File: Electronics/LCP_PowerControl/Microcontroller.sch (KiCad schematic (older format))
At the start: 24 parts, among them J5 Conn_02x05_Odd_Even, SW1 SW_Push, U3 MSP430FR5989, Y1 32.768kHz

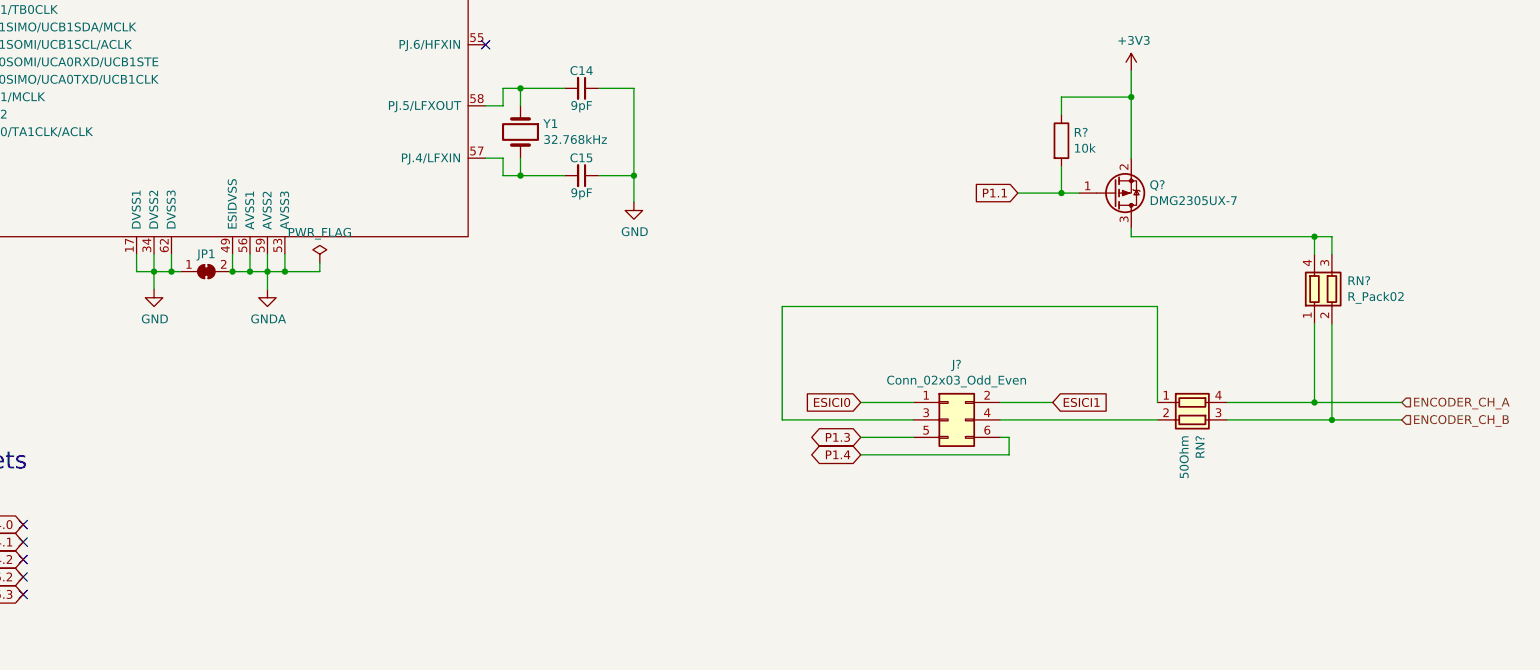
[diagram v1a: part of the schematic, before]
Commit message: Rev1.1 Gerber Upload
Included 3way open solder jumps to choose control of Encoder channels of hall effect sensor
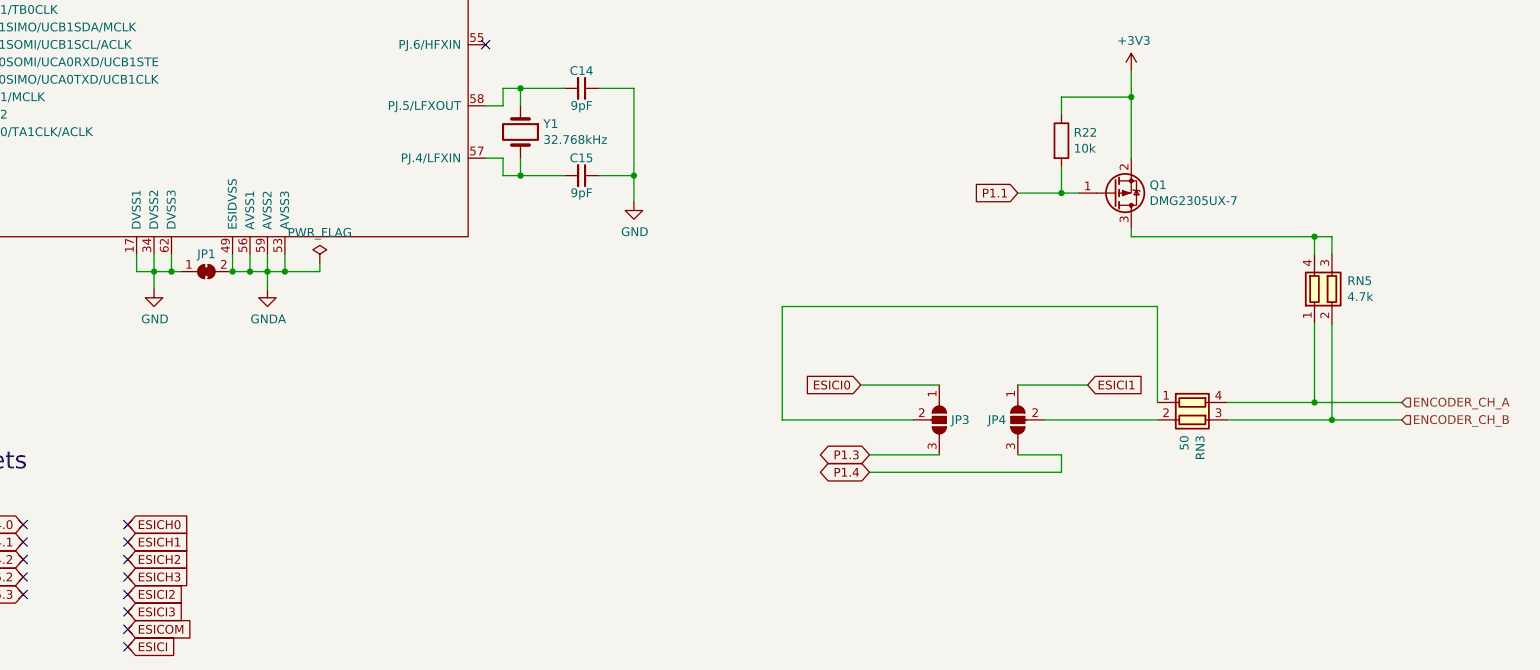
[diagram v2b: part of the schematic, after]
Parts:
- removed J?: Conn_02x03_Odd_Even, Connector_PinHeader_2.54mm:PinHeader_2x03_P2.54mm_Vertical, symbol Connector_Generic:Conn_02x03_Odd_Even
- added JP3, JP4: SolderJumper_3_Open, Jumper:SolderJumper-3_P1.3mm_Open_RoundedPad1.0x1.5mm_NumberLabels, symbol Jumper:SolderJumper_3_Open
- Q1: renamed from Q?; Field4 (none) -> DMG2305UX-7
- RN3: renamed from RN?; value 50Ohm -> 50
- RN5: renamed from RN?; value R_Pack02 -> 4.7k
- gave numbers to parts that had none: 1
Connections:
- net ESICI0: now also JP3.1 (A)
- net ESICI1: now also JP4.1 (A)
- net P1.3: now also JP3.3 (B)
- net P1.4: now also JP4.3 (B)
- net at RN3.1 (R1.1): now also JP3.2 (C)
- net at RN3.2 (R2.1): now also JP4.2 (C)
- no-connect marks 13 -> 21
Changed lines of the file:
@@
 Text HLabel 15150 8150 2    50   Input ~ 0
 ENCODER_CH_B
-Text GLabel 12050 8050 0    50   Input ~ 0
+Text GLabel 12050 7950 0    50   Input ~ 0
 ESICI0
-Text GLabel 13150 8050 2    50   Input ~ 0
+Text GLabel 13350 7950 2    50   Input ~ 0
 ESICI1
 Text GLabel 4350 5550 2    50   Input ~ 0
@@
 Text GLabel 7250 9150 0    50   BiDi ~ 0
 P5.3
-Text GLabel 12050 8350 0    50   BiDi ~ 0
+Text GLabel 12100 8450 0    50   BiDi ~ 0
 P1.4
 Text GLabel 10150 3950 2    50   BiDi ~ 0
@@
 Text GLabel 6750 8950 0    50   BiDi ~ 0
 P2.7
-Text GLabel 12050 8250 0    50   BiDi ~ 0
+Text GLabel 12100 8350 0    50   BiDi ~ 0
 P1.3
 Text GLabel 6450 4600 0    50   BiDi ~ 0
@@
 Wire Wire Line
 	6650 4150 6500 4150
-$Comp
-L Connector_Generic:Conn_02x03_Odd_Even J?
-U 1 1 60479EE2
-P 12550 8150
-F 0 "J?" H 12600 8467 50  0000 C CNN
-F 1 "Conn_02x03_Odd_Even" H 12600 8376 50  0000 C CNN
-F 2 "Connector_PinHeader_2.54mm:PinHeader_2x03_P2.54mm_Vertical" H 12550 8150 50  0001 C CNN
-F 3 "~" H 12550 8150 50  0001 C CNN
-	1    12550 8150
-	1    0    0    -1
-$EndComp
-Wire Wire Line
-	12050 8050 12350 8050
-Wire Wire Line
-	13150 8050 12850 8050
-$Comp
-L Device:R_Pack02 RN?
+Wire Wire Line
+	12050 7950 12500 7950
+$Comp
+L Device:R_Pack02 RN3
 U 1 1 604C7193
 P 13950 8150
-F 0 "RN?" H 14038 8196 50  0000 L CNN
-F 1 "50Ohm" H 14038 8105 50  0000 L CNN
+F 0 "RN3" H 14038 8196 50  0000 L CNN
+F 1 "50" H 14038 8105 50  0000 L CNN
 F 2 "Resistor_SMD:R_Array_Concave_2x0603" V 14125 8150 50  0001 C CNN
 F 3 "~" H 13950 8150 50  0001 C CNN
@@
 $EndComp
 Wire Wire Line
-	12350 8250 12050 8250
-Wire Wire Line
-	12050 8350 12900 8350
-Wire Wire Line
-	12900 8350 12900 8250
-Wire Wire Line
-	12900 8250 12850 8250
-Wire Wire Line
-	13750 8150 12850 8150
+	12500 8350 12100 8350
+Wire Wire Line
+	12100 8450 13200 8450
+Wire Wire Line
+	13200 8450 13200 8350
+Wire Wire Line
+	13200 8350 12950 8350
 Wire Wire Line
 	13750 8050 13750 7500
@@
 	11600 8150 12350 8150
 $Comp
-L Transistor_FET:DMG2301L Q?
+L Transistor_FET:DMG2301L Q1
 U 1 1 604912AC
 P 13500 6850
-F 0 "Q?" H 13705 6804 50  0000 L CNN
+F 0 "Q1" H 13705 6804 50  0000 L CNN
 F 1 "DMG2305UX-7" H 13705 6895 50  0000 L CNN
 F 2 "Package_TO_SOT_SMD:SOT-23" H 13700 6775 50  0001 L CIN
 F 3 "https://www.diodes.com/assets/Datasheets/DMG2305UX.pdf" H 13500 6850 50  0001 L CNN
+F 4 "DMG2305UX-7" H 13500 6850 50  0001 C CNN "Field4"
 	1    13500 6850
 	1    0    0    1
@@
 	13300 6850 13200 6850
 $Comp
-L Device:R_Pack02 RN?
+L Device:R_Pack02 RN5
 U 1 1 604F4633
 P 14750 7400
-AR Path="/5EE2A5A7/604F4633" Ref="RN?"  Part="1"
+AR Path="/5EE2A5A7/604F4633" Ref="RN5"  Part="1"
 AR Path="/5EE7B8CC/604F4633" Ref="RN?"  Part="1"
-F 0 "RN?" H 14838 7446 50  0000 L CNN
-F 1 "R_Pack02" H 14838 7355 50  0000 L CNN
+F 0 "RN5" H 14838 7446 50  0000 L CNN
+F 1 "4.7k" H 14838 7355 50  0000 L CNN
 F 2 "Resistor_SMD:R_Array_Concave_2x0603" V 14925 7400 50  0001 C CNN
 F 3 "~" H 14750 7400 50  0001 C CNN
@@
 	14650 7100 14650 7200
 $Comp
-L power:+3V3 #PWR?
+L power:+3V3 #PWR030
 U 1 1 604F4639
 P 13600 6150
-AR Path="/5EE2A5A7/604F4639" Ref="#PWR?"  Part="1"
+AR Path="/5EE2A5A7/604F4639" Ref="#PWR030"  Part="1"
 AR Path="/5EE7B8CC/604F4639" Ref="#PWR?"  Part="1"
-F 0 "#PWR?" H 13600 6000 50  0001 C CNN
+F 0 "#PWR030" H 13600 6000 50  0001 C CNN
 F 1 "+3V3" H 13615 6323 50  0000 C CNN
 F 2 "" H 13600 6150 50  0001 C CNN
@@
 P 13200 6550
 AR Path="/5EE2AB43/605237E3" Ref="R?"  Part="1"
-AR Path="/5EE2A5A7/605237E3" Ref="R?"  Part="1"
-F 0 "R?" H 13270 6596 50  0000 L CNN
+AR Path="/5EE2A5A7/605237E3" Ref="R22"  Part="1"
+F 0 "R22" H 13270 6596 50  0000 L CNN
 F 1 "10k" H 13270 6505 50  0000 L CNN
 F 2 "Resistor_SMD:R_0805_2012Metric" V 13130 6550 50  0001 C CNN
@@
 Wire Wire Line
 	14750 8150 15150 8150
+$Comp
+L Jumper:SolderJumper_3_Open JP3
+U 1 1 6049AC33
+P 12500 8150
+F 0 "JP3" V 12500 8218 50  0000 L CNN
+F 1 "SolderJumper_3_Open" V 12545 8218 50  0001 L CNN
+F 2 "Jumper:SolderJumper-3_P1.3mm_Open_RoundedPad1.0x1.5mm_NumberLabels" H 12500 8150 50  0001 C CNN
+F 3 "~" H 12500 8150 50  0001 C CNN
+	1    12500 8150
+	0    1    1    0
+$EndComp
+$Comp
+L Jumper:SolderJumper_3_Open JP4
+U 1 1 6049C3B9
+P 12950 8150
+F 0 "JP4" V 12950 8217 50  0000 L CNN
+F 1 "SolderJumper_3_Open" V 12905 8217 50  0001 L CNN
+F 2 "Jumper:SolderJumper-3_P1.3mm_Open_RoundedPad1.0x1.5mm_NumberLabels" H 12950 8150 50  0001 C CNN
+F 3 "~" H 12950 8150 50  0001 C CNN
+	1    12950 8150
+	0    -1   1    0
+$EndComp
+Wire Wire Line
+	12950 7950 13350 7950
+Wire Wire Line
+	13100 8150 13750 8150
+Text GLabel 7850 8750 2    50   Input ~ 0
+ESICH0
+Text GLabel 7850 8850 2    50   Input ~ 0
+ESICH1
+Text GLabel 7850 8950 2    50   Input ~ 0
+ESICH2
+Text GLabel 7850 9050 2    50   Input ~ 0
+ESICH3
+Text GLabel 7850 9150 2    50   Input ~ 0
+ESICI2
+Text GLabel 7850 9250 2    50   Input ~ 0
+ESICI3
+Text GLabel 7850 9450 2    50   Input ~ 0
+ESICI
+Text GLabel 7850 9350 2    50   Input ~ 0
+ESICOM
+NoConn ~ 7850 8750
+NoConn ~ 7850 8850
+NoConn ~ 7850 8950
+NoConn ~ 7850 9050
+NoConn ~ 7850 9150
+NoConn ~ 7850 9250
+NoConn ~ 7850 9350
+NoConn ~ 7850 9450
 $EndSCHEMATC

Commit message: LCP PowerControl Board Update
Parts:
- removed RN3: 50, Resistor_SMD:R_Array_Concave_2x0603, symbol Device:R_Pack02
- added R23, R24: 49.9, Resistor_SMD:R_0805_2012Metric, symbol Device:R
- Q1: Field4 DMG2305UX-7 -> (none); MPN (none) -> DMG2305UX-7
- SW1: MPN PTS810 SJS 250 SMTR LFS -> TL3315NF100Q
- Y1: MPN ABS07-32.768KHZ-9-T -> ABS07-32.768KHZ-9-H-T
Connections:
- net ENCODER_CH_A: now also R23.1
- net ENCODER_CH_B: now also R24.2
- net at JP3.2 (C): now also R23.2
- net at JP4.2 (C): now also R24.1
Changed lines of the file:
@@
 F 2 "Crystal:Crystal_SMD_3215-2Pin_3.2x1.5mm" H 10100 6500 50  0001 C CNN
 F 3 "~" H 10100 6500 50  0001 C CNN
-F 4 "ABS07-32.768KHZ-9-T" V 10100 6500 50  0001 C CNN "MPN"
+F 4 "ABS07-32.768KHZ-9-H-T" V 10100 6500 50  0001 C CNN "MPN"
 	1    10100 6500
 	0    1    1    0
@@
 F 2 "Button_Switch_SMD:SW_SPST_TL3305A" H 12650 3700 50  0001 C CNN
 F 3 "~" H 12650 3700 50  0001 C CNN
-F 4 "PTS810 SJS 250 SMTR LFS" H 12650 3500 50  0001 C CNN "MPN"
+F 4 "TL3315NF100Q" H 12650 3500 50  0001 C CNN "MPN"
 	1    12650 3500
 	1    0    0    -1
@@
 Wire Wire Line
 	12050 7950 12500 7950
-$Comp
-L Device:R_Pack02 RN3
-U 1 1 604C7193
-P 13950 8150
-F 0 "RN3" H 14038 8196 50  0000 L CNN
-F 1 "50" H 14038 8105 50  0000 L CNN
-F 2 "Resistor_SMD:R_Array_Concave_2x0603" V 14125 8150 50  0001 C CNN
-F 3 "~" H 13950 8150 50  0001 C CNN
-F 4 "EXB-V4V510JV" H 13950 8150 50  0001 C CNN "MPN"
-	1    13950 8150
-	0    1    1    0
-$EndComp
 Wire Wire Line
 	12500 8350 12100 8350
@@
 F 2 "Package_TO_SOT_SMD:SOT-23" H 13700 6775 50  0001 L CIN
 F 3 "https://www.diodes.com/assets/Datasheets/DMG2305UX.pdf" H 13500 6850 50  0001 L CNN
-F 4 "DMG2305UX-7" H 13500 6850 50  0001 C CNN "Field4"
+F 4 "DMG2305UX-7" H 13500 6850 50  0001 C CNN "MPN"
 	1    13500 6850
 	1    0    0    1
@@
 Wire Wire Line
 	12950 7950 13350 7950
-Wire Wire Line
-	13100 8150 13750 8150
 Text GLabel 7850 8750 2    50   Input ~ 0
 ESICH0
@@
 NoConn ~ 7850 9350
 NoConn ~ 7850 9450
+$Comp
+L Device:R R23
+U 1 1 6148C867
+P 14000 8050
+F 0 "R23" V 13793 8050 50  0000 C CNN
+F 1 "49.9" V 13900 8050 50  0000 C CNN
+F 2 "Resistor_SMD:R_0805_2012Metric" V 13930 8050 50  0001 C CNN
+F 3 "~" H 14000 8050 50  0001 C CNN
+F 4 "RNCP0805FTD49R9" V 14000 8050 50  0001 C CNN "MPN"
+	1    14000 8050
+	0    1    1    0
+$EndComp
+$Comp
+L Device:R R24
+U 1 1 6148D116
+P 14000 8150
+F 0 "R24" V 13750 8150 50  0000 C CNN
+F 1 "49.9" V 13850 8150 50  0000 C CNN
+F 2 "Resistor_SMD:R_0805_2012Metric" V 13930 8150 50  0001 C CNN
+F 3 "~" H 14000 8150 50  0001 C CNN
+F 4 "RNCP0805FTD49R9" V 14000 8150 50  0001 C CNN "MPN"
+	1    14000 8150
+	0    -1   -1   0
+$EndComp
+Wire Wire Line
+	13750 8050 13850 8050
+Wire Wire Line
+	13100 8150 13850 8150
 $EndSCHEMATC
